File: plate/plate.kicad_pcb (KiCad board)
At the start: 2 copper layers, 143.8 x 126.3 mm, 34 parts, among them SW0 SW_Push, SW1 SW_Push, SW10 SW_Push, SW11 SW_Push, SW12 SW_Push, SW13 SW_Push, SW14 SW_Push, SW15 SW_Push, SW2 SW_Push, SW20 SW_Push, SW21 SW_Push, SW22 SW_Push, SW23 SW_Push, SW24 SW_Push, SW25 SW_Push, SW3 SW_Push, SW30 SW_Push, SW31 SW_Push, SW32 SW_Push, SW33 SW_Push, SW34 SW_Push, SW35 SW_Push, SW4 SW_Push, SW40 SW_Push, SW41 SW_Push, SW42 SW_Push, SW43 SW_Push, SW44 SW_Push, SW45 SW_Push, SW5 SW_Push, SW50 SW_Push

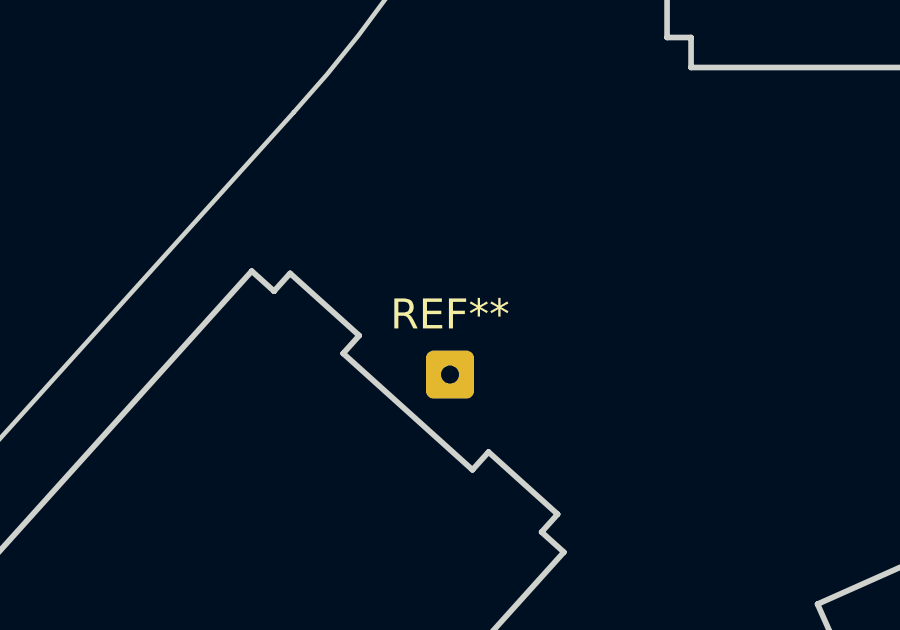
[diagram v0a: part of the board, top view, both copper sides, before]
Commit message: update footprint of rf module
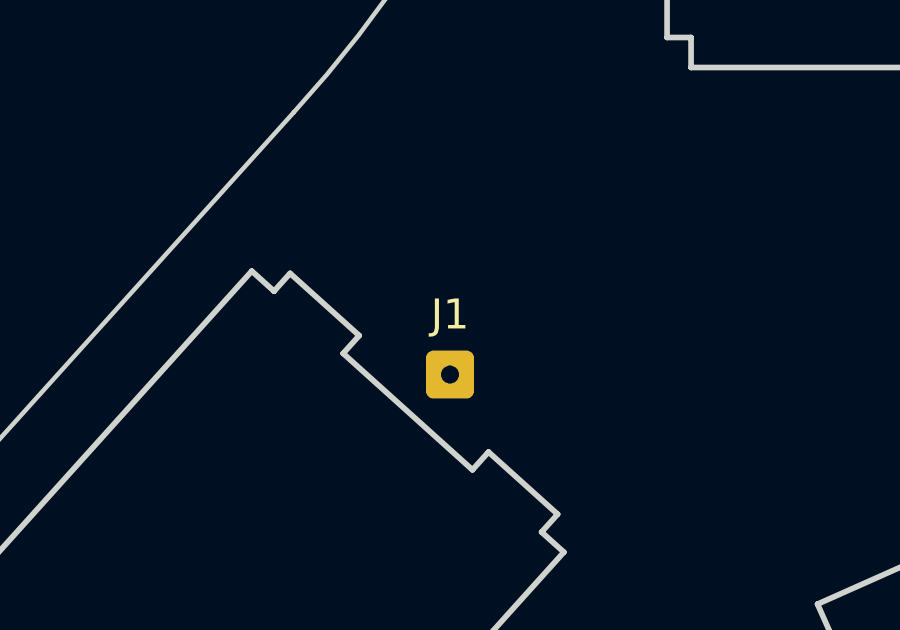
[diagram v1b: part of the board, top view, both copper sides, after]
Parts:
- removed REF**: SolderWire-0.1sqmm_1x01_D0.4mm_OD1mm, Connector_Wire:SolderWire-0.1sqmm_1x01_D0.4mm_OD1mm
- added J1: Conn_01x01, Connector_Wire:SolderWire-0.1sqmm_1x01_D0.4mm_OD1mm, F.Cu at (20.3, 81.2)
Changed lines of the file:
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@@
       (plotinvisibletext false)
       (sketchpadsonfab false)
-      (subtractmaskfromsilk false)
+      (subtractmaskfromsilk true)
       (outputformat 1)
       (mirror false)
@@
   )
   (net 0 "")
+  (net 1 "unconnected-(J1-Pad1)")
   (footprint "blackwing:CUTOUT_CHERRY_MX_1.00u" (layer "F.Cu")
     (at 127.84507 73.752435 180)
@@
     (descr "Soldered wire connection, for a single 0.1 mm² wire, basic insulation, conductor diameter 0.4mm, outer diameter 1mm, size source Multi-Contact FLEXI-E 0.1 (https://ec.staubli.com/AcroFiles/Catalogues/TM_Cab-Main-11014119_(en)_hi.pdf), bend radius 3 times outer diameter, generated with kicad-footprint-generator")
     (tags "connector wire 0.1sqmm")
-    (attr exclude_from_pos_files exclude_from_bom)
-    (fp_text reference "REF**" (at 0 -2) (layer "F.SilkS")
+    (property "Sheetfile" "plate.kicad_sch")
+    (property "Sheetname" "")
+    (attr exclude_from_pos_files)
+    (fp_text reference "J1" (at 0 -2) (layer "F.SilkS")
       (effects (font (size 1 1) (thickness 0.15)))
     )
-    (fp_text value "SolderWire-0.1sqmm_1x01_D0.4mm_OD1mm" (at 0 2) (layer "F.Fab")
+    (fp_text value "Conn_01x01" (at 0 2) (layer "F.Fab")
       (effects (font (size 1 1) (thickness 0.15)))
     )
@@
     )
     (fp_line (start -1.3 1.3) (end 1.3 1.3) (layer "F.CrtYd") (width 0.05))
+    (fp_line (start -1.3 -1.3) (end -1.3 1.3) (layer "F.CrtYd") (width 0.05))
     (fp_line (start 1.3 -1.3) (end -1.3 -1.3) (layer "F.CrtYd") (width 0.05))
-    (fp_line (start -1.3 -1.3) (end -1.3 1.3) (layer "F.CrtYd") (width 0.05))
     (fp_line (start 1.3 1.3) (end 1.3 -1.3) (layer "F.CrtYd") (width 0.05))
     (fp_circle (center 0 0) (end 0.5 0) (layer "F.Fab") (width 0.1) (fill none))
-    (pad "1" thru_hole roundrect locked (at 0 0) (size 1.6 1.6) (drill 0.6) (layers *.Cu *.Mask) (roundrect_rratio 0.15625))
+    (pad "1" thru_hole roundrect locked (at 0 0) (size 1.6 1.6) (drill 0.6) (layers *.Cu *.Mask) (roundrect_rratio 0.15625)
+      (net 1 "unconnected-(J1-Pad1)") (pinfunction "Pin_1"))
     (model "${KICAD6_3DMODEL_DIR}/Connector_Wire.3dshapes/SolderWire-0.1sqmm_1x01_D0.4mm_OD1mm.wrl"
       (offset (xyz 0 0 0))
@@
   (gr_line (start 25.88507 -7.327564) (end 82.885072 -7.327563) (layer "Edge.Cuts") (width 0.15))
   (gr_arc (start 63.88507 141.866421) (end 63.88507 97.172437) (angle -48) (layer "Edge.Cuts") (width 0.15))
-  (target plus (at 25.885071 -2.577564) (size 5) (width 0.15) (layer "Edge.Cuts"))
   (zone (net 0) (net_name "") (layers F&B.Cu) (hatch edge 0.508)
     (connect_pads (clearance 0))
